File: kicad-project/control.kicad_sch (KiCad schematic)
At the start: 28 parts, among them SW1 RST_SW, U1 RP2040

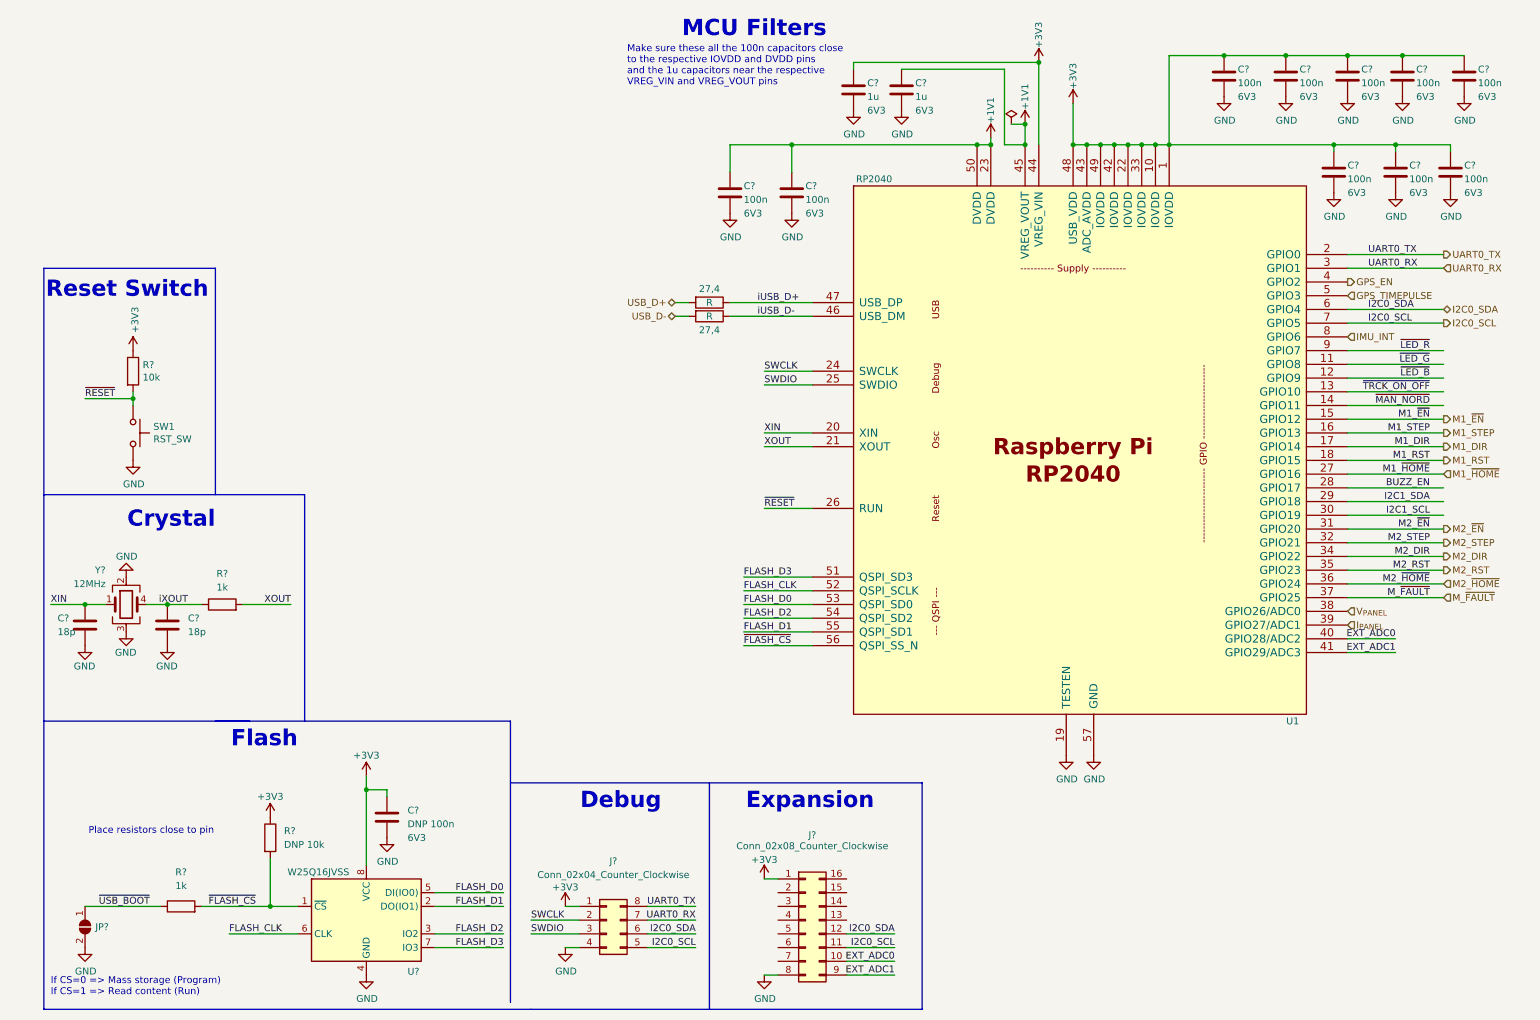
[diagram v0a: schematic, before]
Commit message: hw: add footprints for resistors and capacitors and re-add specs documant that was deleted
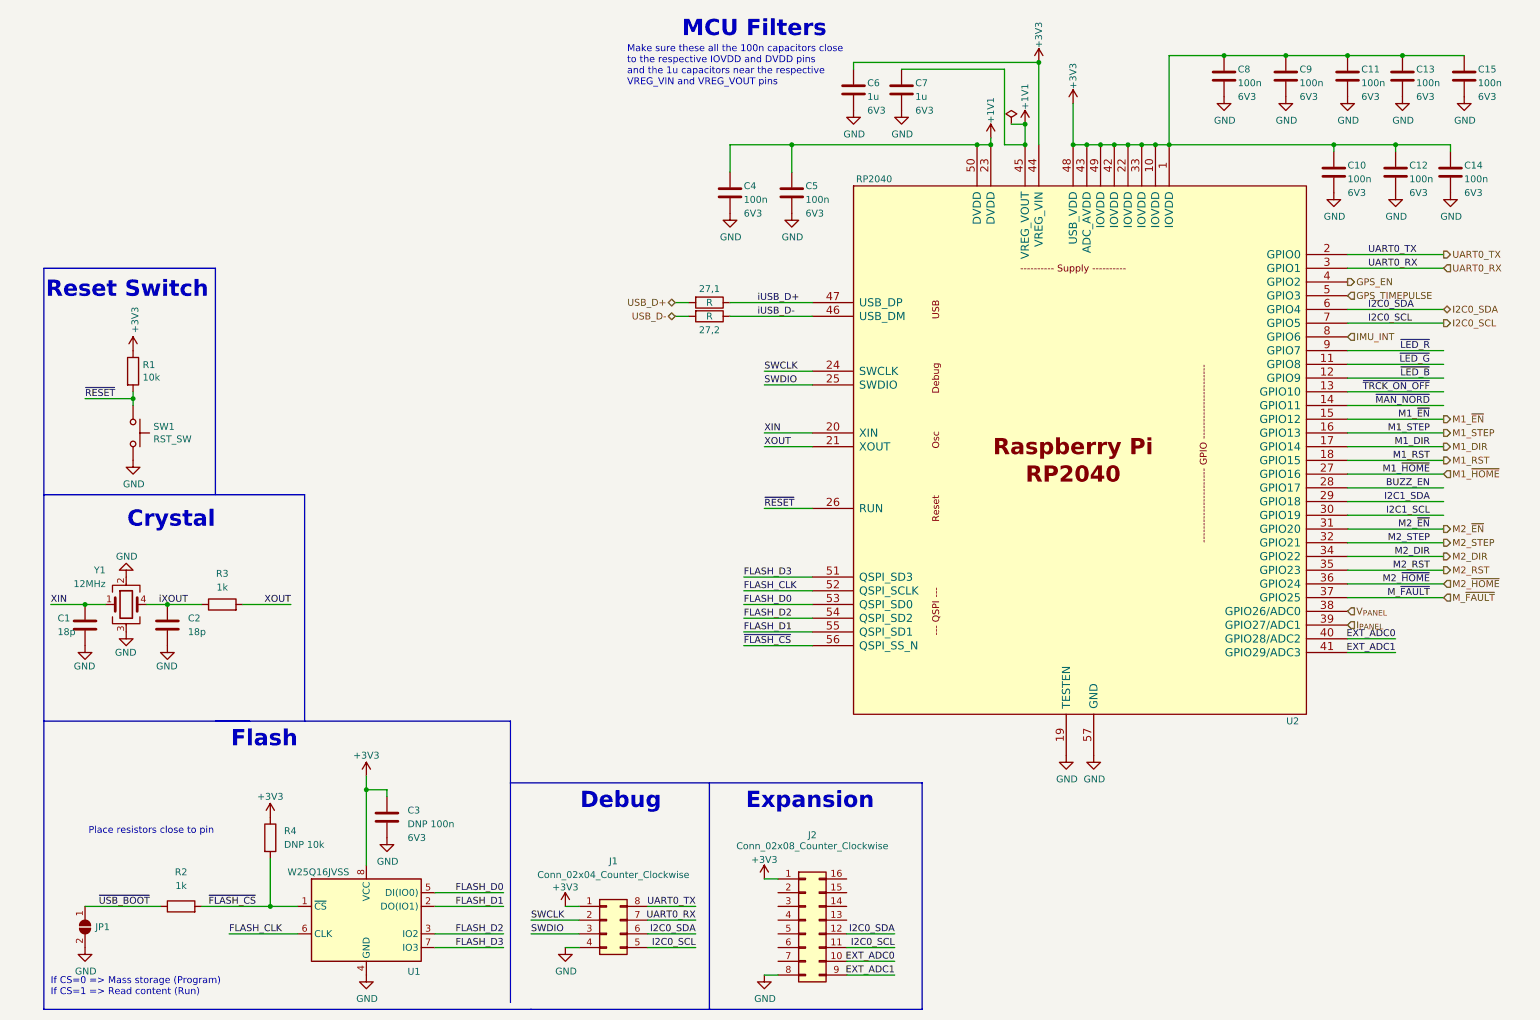
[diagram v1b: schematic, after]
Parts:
- C1, C10, C11, C12, C13, C14, C15, C2, C3, C4, C5, C8, C9: renamed from C?; footprint (none) -> Capacitor_SMD:C_0603_1608Metric
- C6, C7: renamed from C?; footprint (none) -> Capacitor_SMD:C_0805_2012Metric
- J1: renamed from J?; footprint (none) -> Connector_PinHeader_2.54mm:PinHeader_2x04_P2.54mm_Vertical_SMD
- J2: renamed from J?; footprint (none) -> Connector_PinHeader_2.54mm:PinHeader_2x08_P2.54mm_Vertical_SMD
- JP1: renamed from JP?; footprint (none) -> Jumper:SolderJumper-3_P1.3mm_Open_RoundedPad1.0x1.5mm
- R1, R2, R3, R4: renamed from R?; footprint (none) -> Resistor_SMD:R_0603_1608Metric
- SW1: footprint (none) -> Button_Switch_SMD:SW_SPST_PTS645
- Y1: renamed from Y?; footprint (none) -> Crystal:Crystal_SMD_3225-4Pin_3.2x2.5mm
- gave numbers to parts that had none: 1
- renumbered 27,4 to 27,1, 27,4 to 27,2, U1 to U2

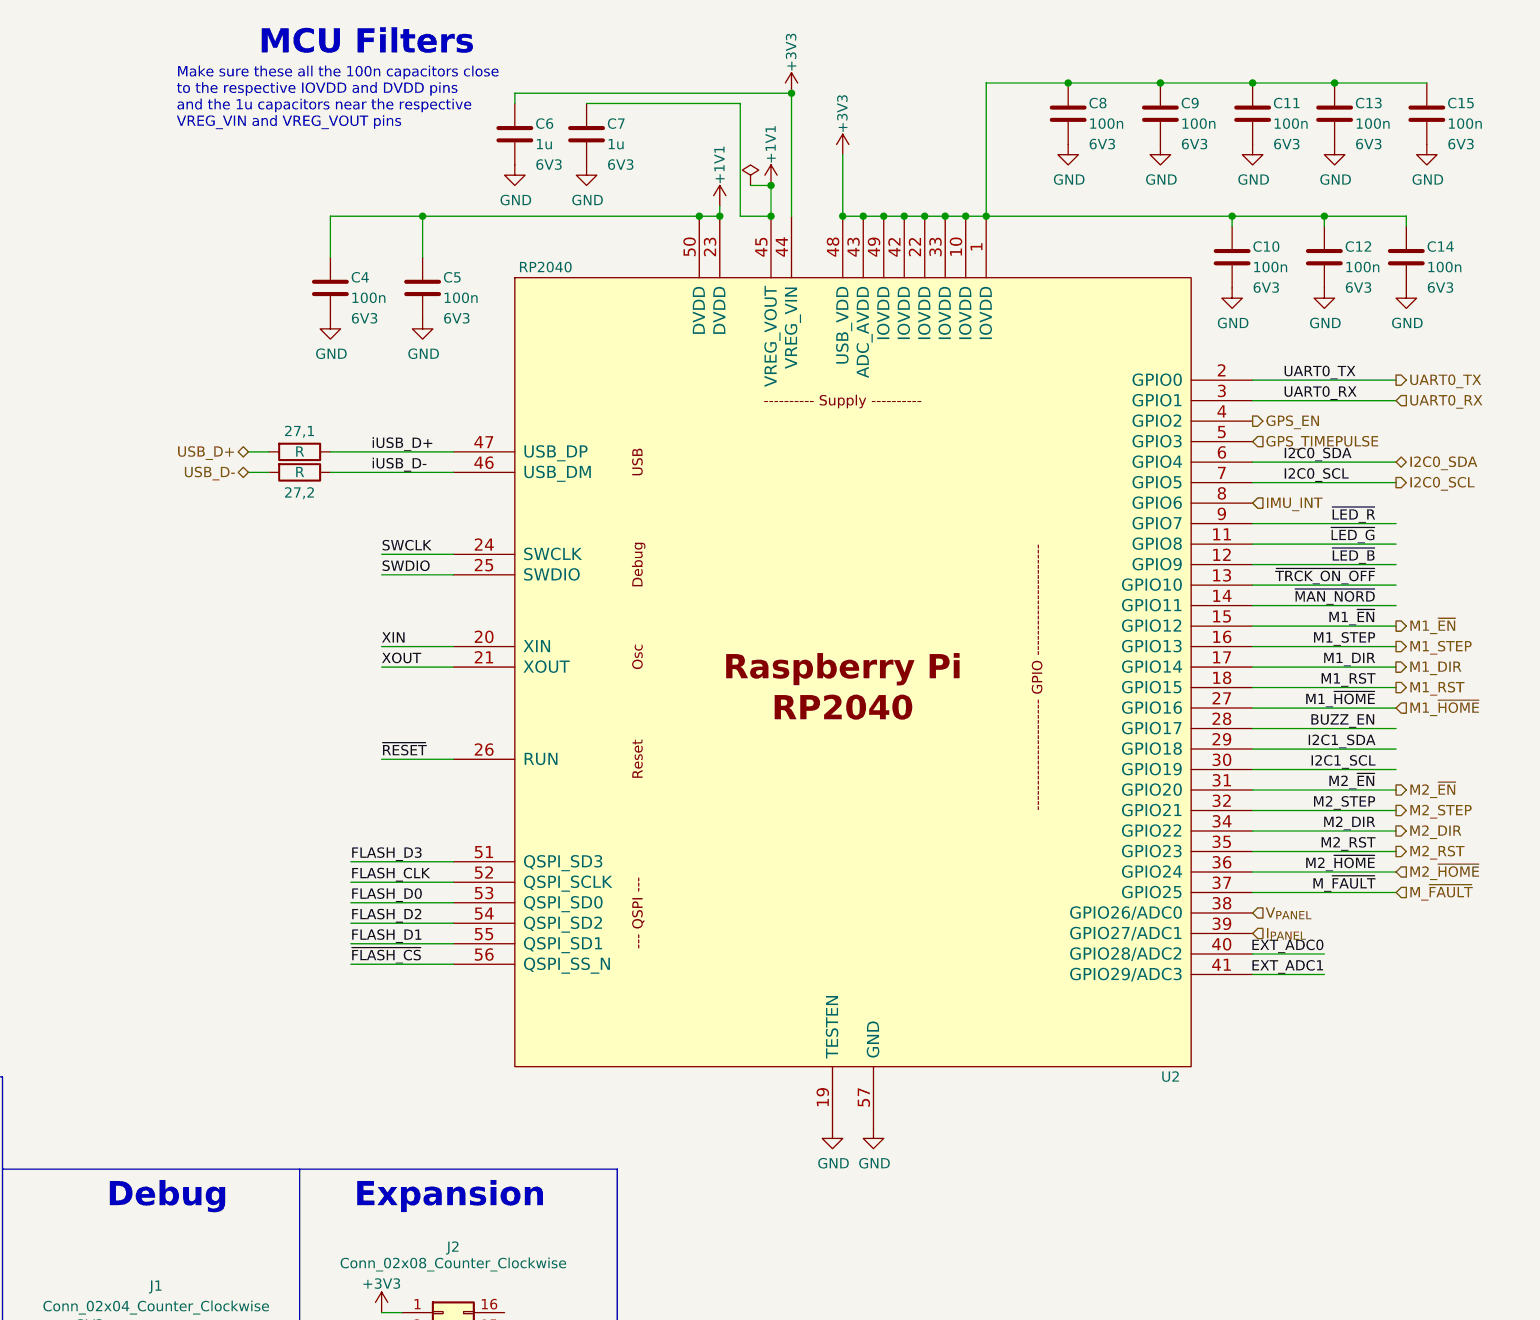
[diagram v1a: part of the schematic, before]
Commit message: hw: update root pin and usb connector
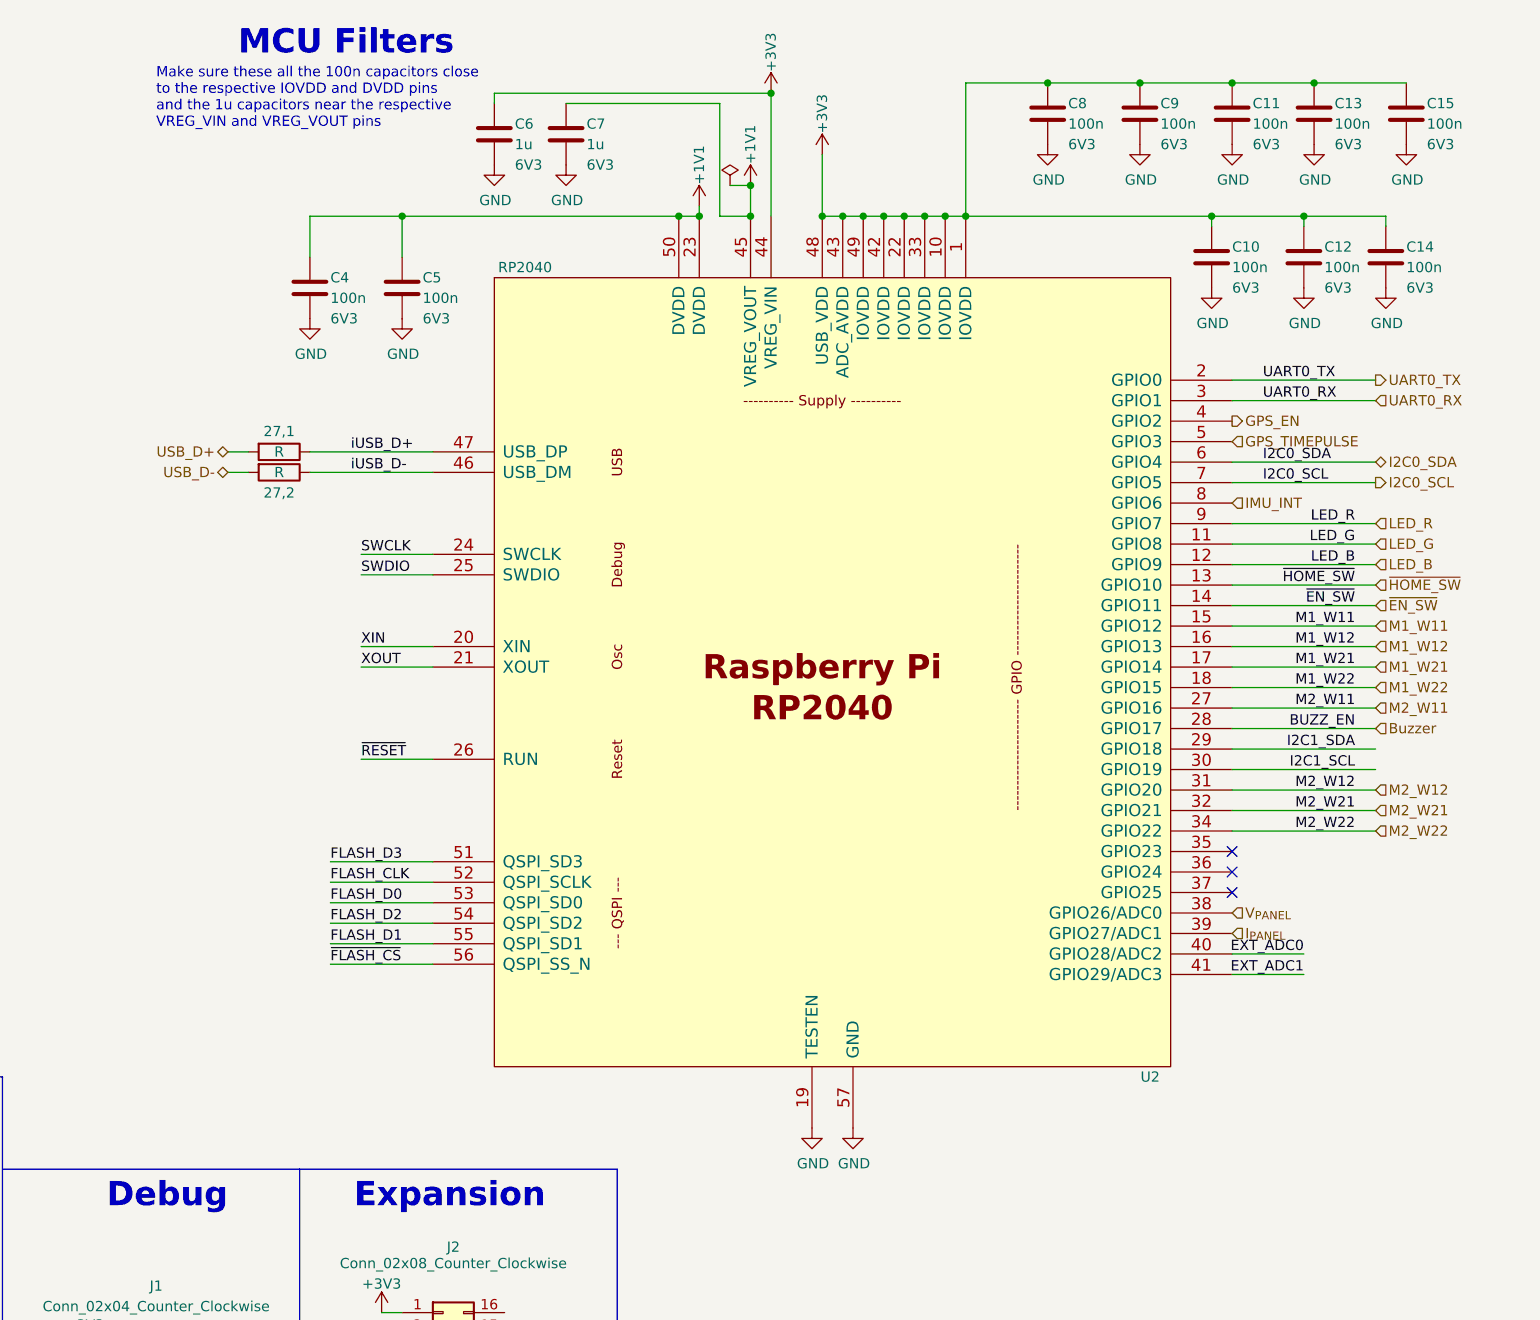
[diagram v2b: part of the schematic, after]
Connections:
- net BUZZ_EN renamed Buzzer
- net M1_DIR renamed M1_W21
- net M1_RST renamed M1_W22
- net M1_STEP renamed M1_W12
- net M1_~{EN} renamed M1_W11
- net M1_~{HOME} renamed M2_W11
- net M2_DIR renamed M2_W22
- net M2_RST: no longer names the net of U2.35 (GPIO23)
- net M2_STEP renamed M2_W21
- net M2_~{EN} renamed M2_W12
- net M2_~{HOME}: no longer names the net of U2.36 (GPIO24)
- net M_~{FAULT}: no longer names the net of U2.37 (GPIO25)
- net ~{LED_B} renamed LED_B
- net ~{LED_G} renamed LED_G
- net ~{LED_R} renamed LED_R
- net ~{MAN_NORD} renamed ~{EN_SW}
- net ~{TRCK_ON_OFF} renamed ~{HOME_SW}
- no-connect marks 0 -> 3
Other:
- moved on the sheet: 27,1, 27,2, C10, C11, C12, C13, C14, C15, C4, C5, C6, C7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

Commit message: hw: part of last checks and footprint assignments
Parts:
- removed JP1: SolderJumper_2_Open, Jumper:SolderJumper-3_P1.3mm_Open_RoundedPad1.0x1.5mm, symbol Jumper:SolderJumper_2_Open
- added C1, C2: 100n, Capacitor_SMD:C_0603_1608Metric, symbol Device:C
- added R1, R2: 10k, Resistor_SMD:R_0603_1608Metric, symbol Device:R
- added SW1: HOME_SW, Button_Switch_SMD:SW_SPST_PTS645, symbol Switch:SW_Push
- added SW2: EN_SW, Button_Switch_SMD:SW_SPST_PTS645, symbol Switch:SW_Push
- added SW3: PRG_SW, Button_Switch_SMD:SW_SPST_PTS645, symbol Switch:SW_Push
- renumbered C8 to C10, C9 to C11, C10 to C12, C11 to C13, C12 to C14, C13 to C15, C14 to C16, C15 to C17, C1 to C3, C2 to C4, C3 to C5, C4 to C6, C5 to C7, C6 to C8, C7 to C9, R1 to R3, R2 to R4, R3 to R5, R4 to R6, SW1 to SW4
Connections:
- net +3V3: now also R1.1, R2.1
- net GND: now also C1.2, C2.2, SW1.2, SW2.2, SW3.2
- net ~{EN_SW}: now also C2.1, R2.2, SW2.1
- net ~{HOME_SW}: now also C1.1, R1.2, SW1.1
- net ~{USB_BOOT}: now also SW3.1
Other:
- note added: "Home Switch"
- note added: "Motor Enable Switch"
- moved on the sheet: R4, R6

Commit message: commit anonimo di thimas
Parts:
- R?: renamed from 27,1; value R -> 27R
- R?: renamed from 27,2; value R -> 27R
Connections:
- net IMU_INT: no longer names the net of U2.8 (GPIO6)
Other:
- note added: "pin da controllare e/o rifare"
- moved on the sheet: C1, C2, R1, R2, SW1, SW2
